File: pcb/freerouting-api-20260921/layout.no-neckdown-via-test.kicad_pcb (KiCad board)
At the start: 4 copper layers, 36 x 76 mm, 115 parts, among them J1 B2B-PH-K-S, J3 B2B-PH-K-S, J4 104031-0811, Q1 AO3400A, Q2 AO3400A, SW1 PTS841GKSMTR LFS, SW2 JS202011AQN, U1 113991114, U10 SN74CBTLV3245APWR, U11 SN74CBTLV3245APWR, U3 MAX17048G+T10, U4 BMI270, U5 TPS61023DRLR, U6 AP2112K-3.3TRG1, U7 TPS22918DBVR, U8 TPS22918DBVR, U9 TPS22918DBVR

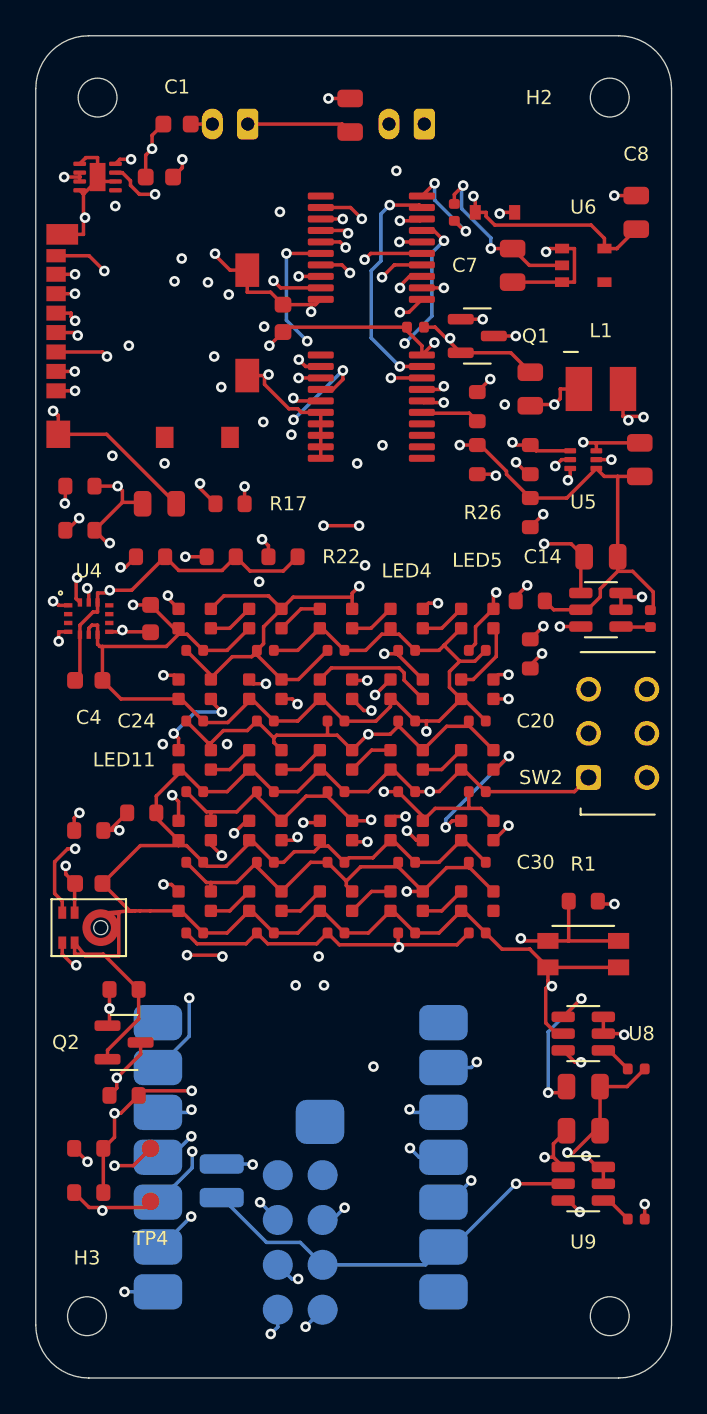
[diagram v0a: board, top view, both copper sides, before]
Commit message: Update board configuration, BOM, and documentation for new XIAO ESP32S3
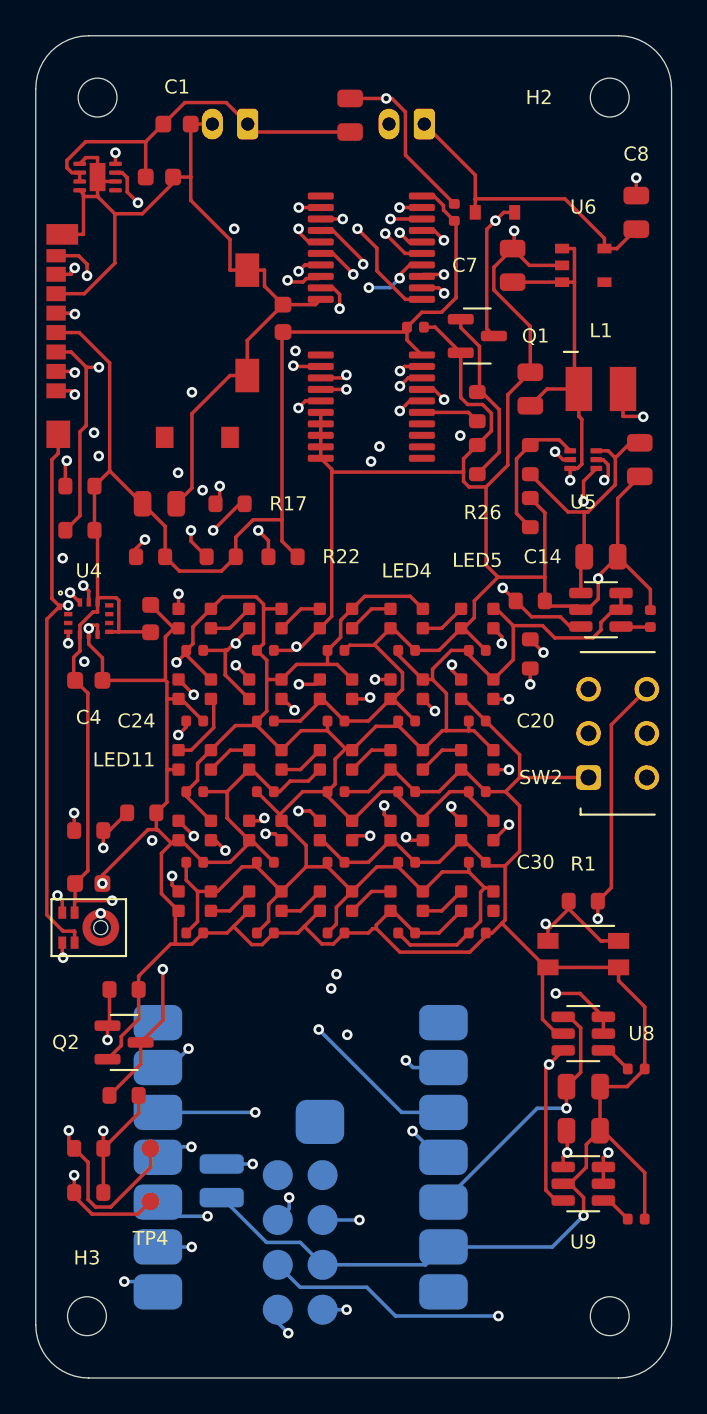
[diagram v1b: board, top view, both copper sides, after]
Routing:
- net GND: track 412.7 -> 474.9 mm, vias 21 -> 12
- net LED_5V: track 175.9 -> 153.2 mm, vias 12 -> 2
- net MCU_EN: track 39.2 -> 49.0 mm
- net FG_SDA: track 92.1 -> 101.1 mm, vias 7 -> 4
- net VBAT: track 110.1 -> 103.4 mm, vias 4 -> 2
- net ISOLATE_N: track 73.0 -> 66.5 mm, vias 4 -> 3
- net IMU_INT: track 34.1 -> 28.2 mm, vias 4 -> 3
- net HOST_LED_ENABLE: track 51.9 -> 57.1 mm, vias 2 -> 3
- net VBAT_PERIPH: track 67.3 -> 62.4 mm, vias 4 -> 2
- net HOST_PDM_CLK: track 63.5 -> 59.0 mm, vias 7 -> 3
- net LED_CHAIN_19: track 10.7 -> 6.39 mm
- net SD_MISO: track 41.6 -> 45.5 mm
- net PDM_CLK_MCU: track 48.1 -> 44.3 mm, vias 4 -> 5
- net HOST_PDM_DATA: track 67.8 -> 64.0 mm, vias 4 -> 2
- net SD_DAT2: track 20.2 -> 16.5 mm, vias 3 -> 2
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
